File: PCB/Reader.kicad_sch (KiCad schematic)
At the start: 42 parts, among them J1 Conn_01x04, J2 Amphenol Dubox ‎76383-402LF‎, J3 Conn_01x04, J4 Conn_01x08, J5 Conn_01x10, J6 Conn_01x03, J7 Conn_01x02, Q1 2N7002, Q2 2N7002, Q3 2N7002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

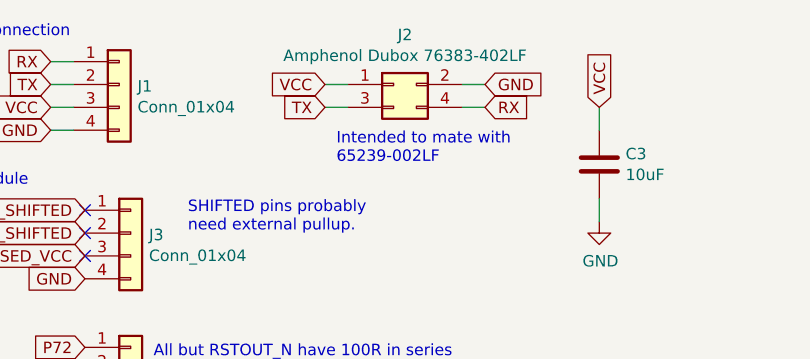
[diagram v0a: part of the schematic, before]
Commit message: ERC: Add power flag for GND and VCC inputs
This fixes the last ERC errors
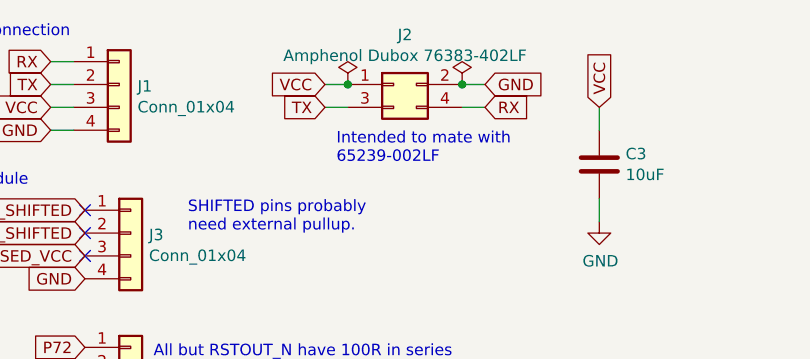
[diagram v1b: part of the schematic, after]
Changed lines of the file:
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@@
 	)
 	(junction
+		(at 76.2 20.32)
+		(diameter 0)
+		(color 0 0 0 0)
+	)
+	(junction
 		(at 180.34 95.25)
 		(diameter 0)
@@
 	)
 	(junction
+		(at 63.5 20.32)
+		(diameter 0)
+		(color 0 0 0 0)
+	)
+	(junction
 		(at 132.08 46.99)
 		(diameter 0)
@@
 	)
 	(symbol
+		(lib_id "power:PWR_FLAG")
+		(at 76.2 20.32 0)
+		(unit 1)
+		(exclude_from_sim no)
+		(in_bom yes)
+		(on_board yes)
+		(dnp no)
+		(fields_autoplaced yes)
+		(property "Reference" "#FLG02"
+			(at 76.2 18.415 0)
+			(effects
+				(font
+					(size 1.27 1.27)
+				)
+				(hide yes)
+			)
+		)
+		(property "Value" "PWR_FLAG"
+			(at 76.2 16.1869 0)
+			(effects
+				(font
+					(size 1.27 1.27)
+				)
+				(hide yes)
+			)
+		)
+		(property "Footprint" ""
+			(at 76.2 20.32 0)
+			(effects
+				(font
+					(size 1.27 1.27)
+				)
+				(hide yes)
+			)
+		)
+		(property "Datasheet" "~"
+			(at 76.2 20.32 0)
+			(effects
+				(font
+					(size 1.27 1.27)
+				)
+				(hide yes)
+			)
+		)
+		(property "Description" "Special symbol for telling ERC where power comes from"
+			(at 76.2 20.32 0)
+			(effects
+				(font
+					(size 1.27 1.27)
+				)
+				(hide yes)
+			)
+		)
+		(pin "1"
+		)
+		(instances
+			(project "Reader"
+				(path "/f5709391-a389-450b-a647-2f06b3cb0d95"
+					(reference "#FLG02")
+					(unit 1)
+				)
+			)
+		)
+	)
+	(symbol
 		(lib_id "Device:R")
 		(at 53.34 173.99 90)
@@
 					(unit 1)
 				)
+			)
+		)
+	)
+	(symbol
+		(lib_id "power:PWR_FLAG")
+		(at 63.5 20.32 0)
+		(unit 1)
+		(exclude_from_sim no)
+		(in_bom yes)
+		(on_board yes)
+		(dnp no)
+		(fields_autoplaced yes)
+		(property "Reference" "#FLG01"
+			(at 63.5 18.415 0)
+			(effects
+				(font
+					(size 1.27 1.27)
+				)
+				(hide yes)
+			)
+		)
+		(property "Value" "PWR_FLAG"
+			(at 63.5 16.1869 0)
+			(effects
+				(font
+					(size 1.27 1.27)
+				)
+				(hide yes)
+			)
+		)
+		(property "Footprint" ""
+			(at 63.5 20.32 0)
+			(effects
+				(font
+					(size 1.27 1.27)
+				)
+				(hide yes)
+			)
+		)
+		(property "Datasheet" "~"
+			(at 63.5 20.32 0)
+			(effects
+				(font
+					(size 1.27 1.27)
+				)
+				(hide yes)
+			)
+		)
+		(property "Description" "Special symbol for telling ERC where power comes from"
+			(at 63.5 20.32 0)
+			(effects
+				(font
+					(size 1.27 1.27)
+				)
+				(hide yes)
+			)
+		)
+		(pin "1"
+		)
+		(instances
+			(project "Reader"
+				(path "/f5709391-a389-450b-a647-2f06b3cb0d95"
+					(reference "#FLG01")
+					(unit 1)
+				)
